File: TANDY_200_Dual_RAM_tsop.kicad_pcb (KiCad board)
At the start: 2 copper layers, 35.6 x 25.4 mm, 5 parts, among them J1 Conn_01x01_Male, J2 TANDY_26-3688, U1 628128_TSOP32, U2 74LVC1G08

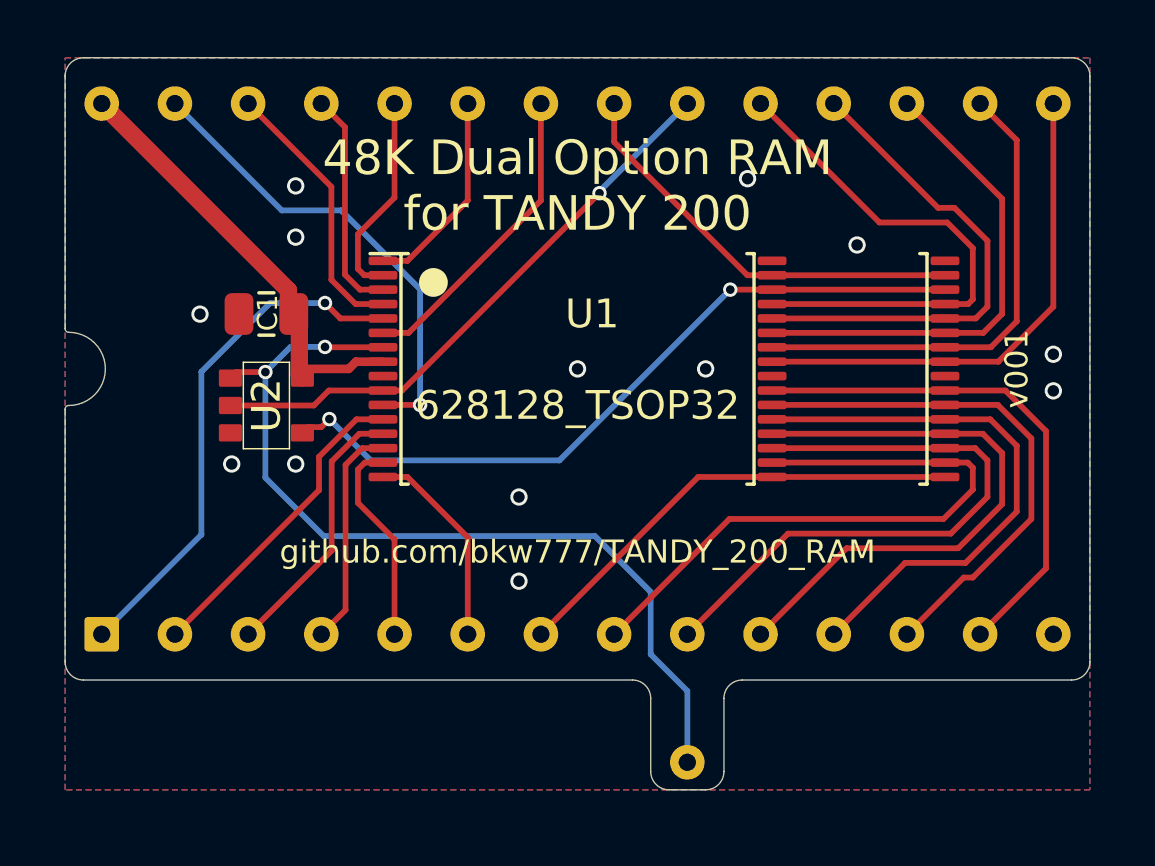
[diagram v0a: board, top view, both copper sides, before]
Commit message: board outlines, ground planes
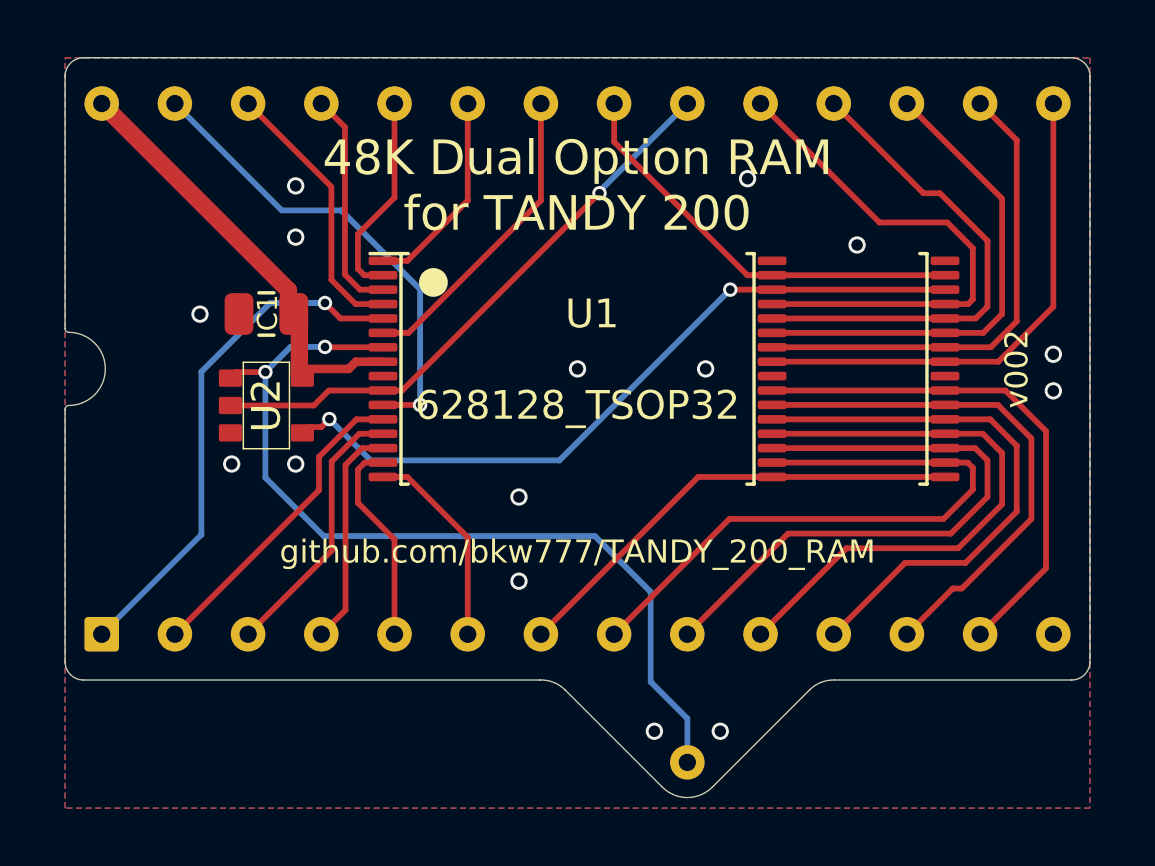
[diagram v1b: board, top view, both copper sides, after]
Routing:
- net GND: vias 13 -> 15
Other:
- board size 35.6 x 25.4 mm -> 35.6 x 25.7 mm
- board text removed: "Row spacing is 725mils, not 700."

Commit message: add single-bank tsop
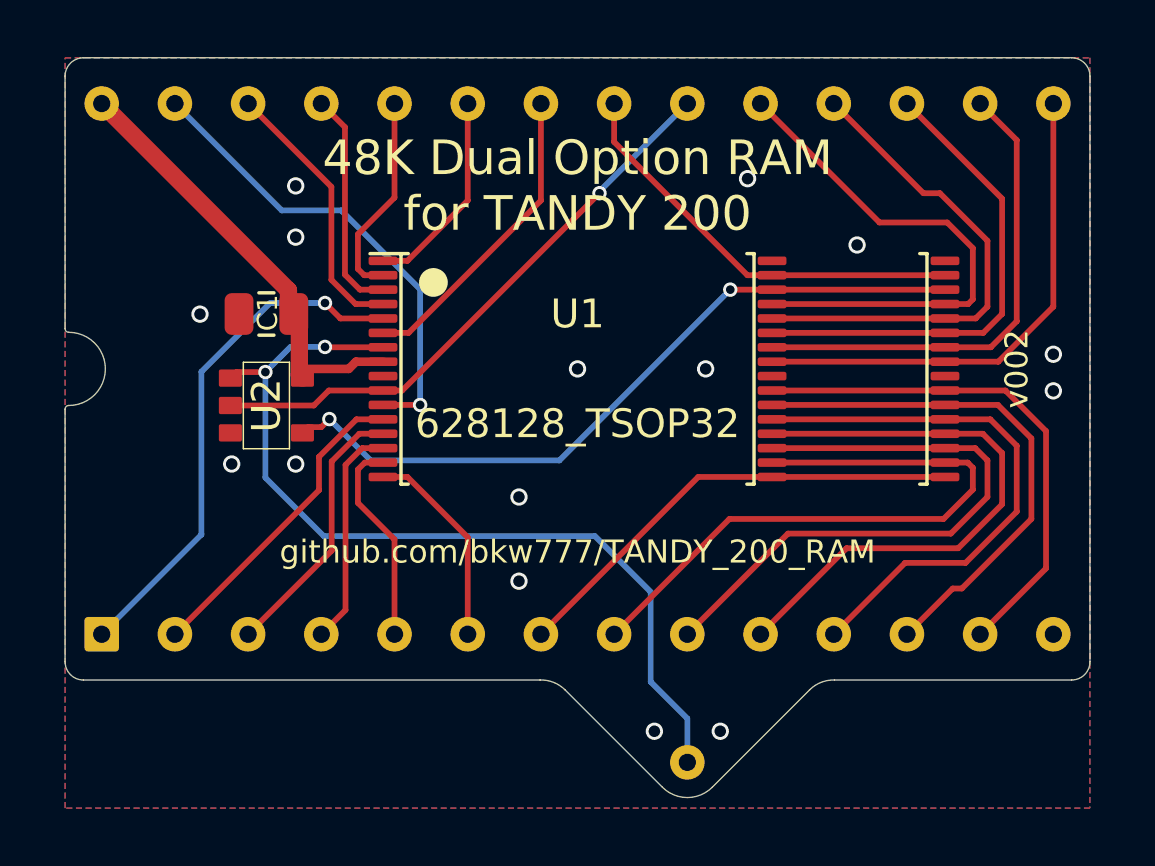
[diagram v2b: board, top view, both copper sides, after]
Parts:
- moved U1 3.00 mm to (150.3, 99.1), turned to 0 degrees

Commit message: ground paths, footprints, sch symbols
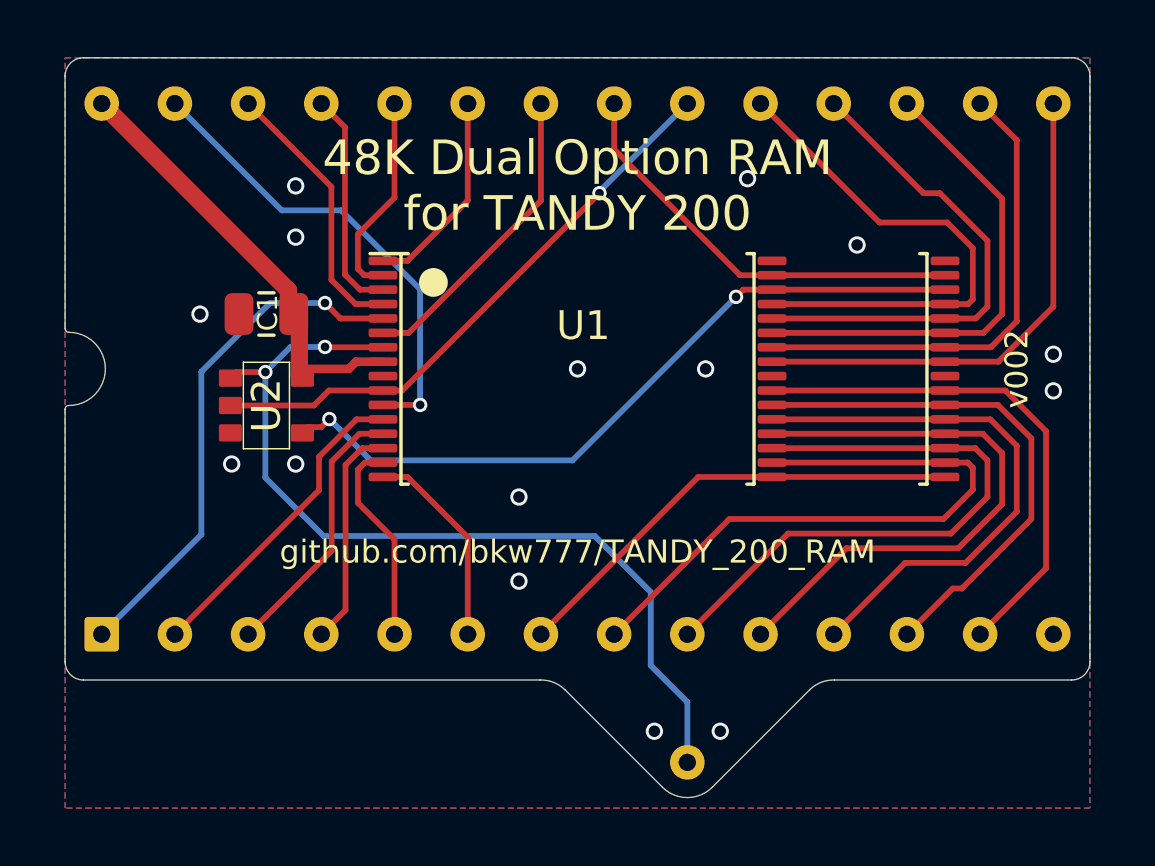
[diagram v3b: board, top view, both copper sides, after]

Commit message: 24k tsop layout and all board outlines expanded slightly
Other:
- board size 35.6 x 25.7 mm -> 36.1 x 25.5 mm
- board text added: "C1: ${91f0851b-88d9-4f00-a08c-ede0bdd24da4:VALUE} U2: ${eda52ffc-b211-43e3-a91c-151a6f13f97e:VALUE} PINS: Mill-Max 3121 or TE 1544210"
- board text removed: "C1: 0.1uF U2: 74LVC1G08 PINS: Mill-Max 3121 or TE 1544210"
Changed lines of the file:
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@@
   (title_block
     (title "TANDY 200 Dual RAM tsop")
-    (date "2022-09-22")
-    (rev "002")
+    (date "2022-10-01")
+    (rev "003")
     (company "b.kenyon.w@gmail.com")
     (comment 1 "github.com/bkw777/TANDY_200_RAM")
@@
     )
   )
-  (gr_line (start 151.993599 113.576099) (end 155.3718 110.197901) (layer "Edge.Cuts") (width 0.01))
-  (gr_arc (start 129.54 100.457) (mid 129.577197 100.367197) (end 129.667 100.33) (layer "Edge.Cuts") (width 0.01))
-  (gr_arc (start 151.993599 113.576099) (mid 151.13 113.933813) (end 150.266401 113.576099) (layer "Edge.Cuts") (width 0.01))
-  (gr_arc (start 165.1 109.22) (mid 164.914013 109.669013) (end 164.465 109.855) (layer "Edge.Cuts") (width 0.01))
-  (gr_arc (start 129.667 97.79) (mid 129.577197 97.752803) (end 129.54 97.663) (layer "Edge.Cuts") (width 0.01))
-  (gr_line (start 129.54 100.457) (end 129.54 109.22) (layer "Edge.Cuts") (width 0.01))
-  (gr_line (start 156.2354 109.855) (end 164.465 109.855) (layer "Edge.Cuts") (width 0.01))
-  (gr_arc (start 129.667 97.79) (mid 130.937 99.06) (end 129.667 100.33) (layer "Edge.Cuts") (width 0.01))
-  (gr_line (start 164.465 88.265) (end 130.175 88.265) (layer "Edge.Cuts") (width 0.01))
-  (gr_line (start 165.1 109.22) (end 165.1 88.9) (layer "Edge.Cuts") (width 0.01))
-  (gr_arc (start 155.3718 110.197901) (mid 155.768182 109.937245) (end 156.2354 109.855) (layer "Edge.Cuts") (width 0.01))
-  (gr_arc (start 129.54 88.9) (mid 129.725987 88.450987) (end 130.175 88.265) (layer "Edge.Cuts") (width 0.01))
-  (gr_line (start 129.54 97.663) (end 129.54 88.9) (layer "Edge.Cuts") (width 0.01))
-  (gr_line (start 146.0246 109.855) (end 130.175 109.855) (layer "Edge.Cuts") (width 0.01))
-  (gr_arc (start 164.465 88.265) (mid 164.914013 88.450987) (end 165.1 88.9) (layer "Edge.Cuts") (width 0.01))
-  (gr_line (start 146.8882 110.197901) (end 150.266401 113.576099) (layer "Edge.Cuts") (width 0.01))
-  (gr_arc (start 130.175 109.855) (mid 129.725987 109.669013) (end 129.54 109.22) (layer "Edge.Cuts") (width 0.01))
-  (gr_arc (start 146.0246 109.855) (mid 146.491818 109.937249) (end 146.8882 110.197901) (layer "Edge.Cuts") (width 0.01))
-  (gr_text "C1: 0.1uF\nU2: 74LVC1G08\nPINS: Mill-Max 3121 or TE 1544210" (at 163.195 103.505) (layer "B.SilkS")
+  (gr_arc (start 129.286 100.457) (mid 129.323197 100.367197) (end 129.413 100.33) (layer "Edge.Cuts") (width 0.01))
+  (gr_line (start 152.032504 113.551504) (end 155.56778 110.02558) (layer "Edge.Cuts") (width 0.01))
+  (gr_arc (start 152.032504 113.551504) (mid 151.13 113.925333) (end 150.227496 113.551504) (layer "Edge.Cuts") (width 0.01))
+  (gr_arc (start 155.56778 110.02558) (mid 155.897394 109.805339) (end 156.2862 109.728001) (layer "Edge.Cuts") (width 0.01))
+  (gr_arc (start 165.354 109.093) (mid 165.168013 109.542013) (end 164.719 109.728) (layer "Edge.Cuts") (width 0.01))
+  (gr_arc (start 145.9738 109.728) (mid 146.362606 109.805338) (end 146.69222 110.02558) (layer "Edge.Cuts") (width 0.01))
+  (gr_arc (start 129.413 97.79) (mid 129.323197 97.752803) (end 129.286 97.663) (layer "Edge.Cuts") (width 0.01))
+  (gr_line (start 129.286 100.457) (end 129.286 109.093) (layer "Edge.Cuts") (width 0.01))
+  (gr_line (start 156.2862 109.728001) (end 164.719 109.728) (layer "Edge.Cuts") (width 0.01))
+  (gr_arc (start 129.413 97.79) (mid 130.683 99.06) (end 129.413 100.33) (layer "Edge.Cuts") (width 0.01))
+  (gr_line (start 164.719 88.392) (end 129.921 88.392) (layer "Edge.Cuts") (width 0.01))
+  (gr_line (start 165.354 109.093) (end 165.354 89.027) (layer "Edge.Cuts") (width 0.01))
+  (gr_line (start 150.227496 113.551504) (end 146.69222 110.02558) (layer "Edge.Cuts") (width 0.01))
+  (gr_arc (start 129.286 89.027) (mid 129.471987 88.577987) (end 129.921 88.392) (layer "Edge.Cuts") (width 0.01))
+  (gr_line (start 129.286 97.663) (end 129.286 89.027) (layer "Edge.Cuts") (width 0.01))
+  (gr_line (start 145.9738 109.728) (end 129.921 109.728) (layer "Edge.Cuts") (width 0.01))
+  (gr_arc (start 164.719 88.392) (mid 165.168013 88.577987) (end 165.354 89.027) (layer "Edge.Cuts") (width 0.01))
+  (gr_arc (start 129.921 109.728) (mid 129.471987 109.542013) (end 129.286 109.093) (layer "Edge.Cuts") (width 0.01))
+  (gr_text "C1: ${91f0851b-88d9-4f00-a08c-ede0bdd24da4:VALUE}\nU2: ${eda52ffc-b211-43e3-a91c-151a6f13f97e:VALUE}\nPINS: Mill-Max 3121 or TE 1544210" (at 163.195 103.505) (layer "B.SilkS")
     (effects (font (size 1 1) (thickness 0.15)) (justify left mirror))
   )
@@
   (segment (start 162.56 104.013) (end 160.782 105.791) (width 0.2) (layer "F.Cu") (net 1))
   (segment (start 158.6865 105.791) (end 156.21 108.2675) (width 0.2) (layer "F.Cu") (net 1))
-  (segment (start 163.068 104.267) (end 160.655 106.68) (width 0.2) (layer "F.Cu") (net 2))
-  (segment (start 160.3375 106.68) (end 158.75 108.2675) (width 0.2) (layer "F.Cu") (net 2))
+  (segment (start 161.905 100.31) (end 163.068 101.473) (width 0.2) (layer "F.Cu") (net 2))
+  (segment (start 163.068 104.267) (end 160.528 106.807) (width 0.2) (layer "F.Cu") (net 2))
+  (segment (start 160.2105 106.807) (end 158.75 108.2675) (width 0.2) (layer "F.Cu") (net 2))
+  (segment (start 160.528 106.807) (end 160.2105 106.807) (width 0.2) (layer "F.Cu") (net 2))
   (segment (start 163.068 101.473) (end 163.068 104.267) (width 0.2) (layer "F.Cu") (net 2))
-  (segment (start 161.905 100.31) (end 163.068 101.473) (width 0.2) (layer "F.Cu") (net 2))
   (segment (start 154.07 100.31) (end 161.905 100.31) (width 0.2) (layer "F.Cu") (net 2))
-  (segment (start 160.655 106.68) (end 160.3375 106.68) (width 0.2) (layer "F.Cu") (net 2))
   (via (at 163.83 99.822) (size 0.6) (drill 0.4) (layers "F.Cu" "B.Cu") (free) (net 3))
   (via (at 137.541 92.71) (size 0.6) (drill 0.4) (layers "F.Cu" "B.Cu") (free) (net 3))
@@
     (polygon
       (pts
-        (xy 165.1 114.3)
-        (xy 129.54 114.3)
-        (xy 129.54 88.265)
-        (xy 165.1 88.265)
+        (xy 165.354 114.3)
+        (xy 129.286 114.3)
+        (xy 129.286 88.265)
+        (xy 165.354 88.265)
       )
     )
@@
     (polygon
       (pts
-        (xy 165.1 114.3)
-        (xy 129.54 114.3)
-        (xy 129.54 88.265)
-        (xy 165.1 88.265)
+        (xy 165.354 114.3)
+        (xy 129.286 114.3)
+        (xy 129.286 88.265)
+        (xy 165.354 88.265)
       )
     )

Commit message: 48k tsop ground pour
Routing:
- net /A14: track 16.5 -> 17.5 mm
- net GND: vias 15 -> 4
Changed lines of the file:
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@@
     (title "TANDY 200 Dual RAM tsop")
     (date "2022-10-01")
-    (rev "003")
+    (rev "004")
     (company "b.kenyon.w@gmail.com")
     (comment 1 "github.com/bkw777/TANDY_200_RAM")
@@
   (segment (start 163.068 101.473) (end 163.068 104.267) (width 0.2) (layer "F.Cu") (net 2))
   (segment (start 154.07 100.31) (end 161.905 100.31) (width 0.2) (layer "F.Cu") (net 2))
-  (via (at 163.83 99.822) (size 0.6) (drill 0.4) (layers "F.Cu" "B.Cu") (free) (net 3))
-  (via (at 137.541 92.71) (size 0.6) (drill 0.4) (layers "F.Cu" "B.Cu") (free) (net 3))
-  (via (at 153.22 92.46) (size 0.6) (drill 0.4) (layers "F.Cu" "B.Cu") (free) (net 3))
-  (via (at 135.32 102.36) (size 0.6) (drill 0.4) (layers "F.Cu" "B.Cu") (free) (net 3))
-  (via (at 145.288 106.426) (size 0.6) (drill 0.4) (layers "F.Cu" "B.Cu") (free) (net 3))
-  (via (at 137.541 102.362) (size 0.6) (drill 0.4) (layers "F.Cu" "B.Cu") (free) (net 3))
-  (via (at 157.02 94.76) (size 0.6) (drill 0.4) (layers "F.Cu" "B.Cu") (free) (net 3))
-  (via (at 163.83 98.552) (size 0.6) (drill 0.4) (layers "F.Cu" "B.Cu") (free) (net 3))
-  (via (at 134.22 97.16) (size 0.6) (drill 0.4) (layers "F.Cu" "B.Cu") (free) (net 3))
-  (via (at 145.288 103.505) (size 0.6) (drill 0.4) (layers "F.Cu" "B.Cu") (free) (net 3))
-  (via (at 152.273 111.633) (size 0.6) (drill 0.4) (layers "F.Cu" "B.Cu") (free) (net 3))
-  (via (at 151.765 99.06) (size 0.6) (drill 0.4) (layers "F.Cu" "B.Cu") (free) (net 3))
-  (via (at 137.541 94.488) (size 0.6) (drill 0.4) (layers "F.Cu" "B.Cu") (free) (net 3))
-  (via (at 149.987 111.633) (size 0.6) (drill 0.4) (layers "F.Cu" "B.Cu") (free) (net 3))
-  (via (at 147.32 99.06) (size 0.6) (drill 0.4) (layers "F.Cu" "B.Cu") (free) (net 3))
+  (via (at 163.83 99.06) (size 0.6) (drill 0.4) (layers "F.Cu" "B.Cu") (free) (net 3))
+  (via (at 134.62 95.885) (size 0.6) (drill 0.4) (layers "F.Cu" "B.Cu") (free) (net 3))
+  (via (at 137.414 102.489) (size 0.6) (drill 0.4) (layers "F.Cu" "B.Cu") (free) (net 3))
+  (via (at 152.4 99.314) (size 0.6) (drill 0.4) (layers "F.Cu" "B.Cu") (free) (net 3))
   (segment (start 163.576 101.219) (end 163.576 105.9815) (width 0.2) (layer "F.Cu") (net 4))
   (segment (start 163.576 105.9815) (end 161.29 108.2675) (width 0.2) (layer "F.Cu") (net 4))
@@
   (segment (start 154.6225 104.775) (end 151.13 108.2675) (width 0.2) (layer "F.Cu") (net 21))
   (segment (start 161.544 103.505) (end 160.274 104.775) (width 0.2) (layer "F.Cu") (net 21))
-  (segment (start 140.57 100.31) (end 141.859 100.31) (width 0.2) (layer "F.Cu") (net 22))
-  (via (at 141.859 100.31) (size 0.5) (drill 0.3) (layers "F.Cu" "B.Cu") (net 22))
-  (segment (start 139.12 93.56) (end 137.0575 93.56) (width 0.2) (layer "B.Cu") (net 22))
-  (segment (start 137.0575 93.56) (end 133.35 89.8525) (width 0.2) (layer "B.Cu") (net 22))
-  (segment (start 141.859 100.31) (end 141.859 96.299) (width 0.2) (layer "B.Cu") (net 22))
-  (segment (start 141.859 96.299) (end 139.12 93.56) (width 0.2) (layer "B.Cu") (net 22))
+  (segment (start 142.748 99.314) (end 141.752 100.31) (width 0.2) (layer "F.Cu") (net 22))
+  (segment (start 141.752 100.31) (end 140.57 100.31) (width 0.2) (layer "F.Cu") (net 22))
+  (via (at 142.748 99.314) (size 0.5) (drill 0.3) (layers "F.Cu" "B.Cu") (net 22))
+  (segment (start 136.8425 93.345) (end 133.35 89.8525) (width 0.2) (layer "B.Cu") (net 22))
+  (segment (start 142.748 96.52) (end 139.573 93.345) (width 0.2) (layer "B.Cu") (net 22))
+  (segment (start 139.573 93.345) (end 136.8425 93.345) (width 0.2) (layer "B.Cu") (net 22))
+  (segment (start 142.748 99.314) (end 142.748 96.52) (width 0.2) (layer "B.Cu") (net 22))
   (segment (start 156.6545 105.283) (end 153.67 108.2675) (width 0.2) (layer "F.Cu") (net 23))
   (segment (start 161.381 101.31) (end 162.052 101.981) (width 0.2) (layer "F.Cu") (net 23))
@@
   (via (at 136.49 99.17) (size 0.5) (drill 0.3) (layers "F.Cu" "B.Cu") (net 25))
   (via (at 138.557 98.298) (size 0.5) (drill 0.3) (layers "F.Cu" "B.Cu") (free) (net 25))
+  (segment (start 149.86 109.35) (end 151.13 110.62) (width 0.2) (layer "B.Cu") (net 25))
+  (segment (start 138.557 98.298) (end 137.362 98.298) (width 0.2) (layer "B.Cu") (net 25))
+  (segment (start 148.343 105.283) (end 149.86 106.8) (width 0.2) (layer "B.Cu") (net 25))
+  (segment (start 138.938 105.283) (end 148.343 105.283) (width 0.2) (layer "B.Cu") (net 25))
+  (segment (start 137.362 98.298) (end 136.49 99.17) (width 0.2) (layer "B.Cu") (net 25))
+  (segment (start 136.49 99.17) (end 136.49 102.835) (width 0.2) (layer "B.Cu") (net 25))
+  (segment (start 149.86 106.8) (end 149.86 109.35) (width 0.2) (layer "B.Cu") (net 25))
+  (segment (start 136.49 102.835) (end 138.938 105.283) (width 0.2) (layer "B.Cu") (net 25))
   (segment (start 151.13 110.62) (end 151.13 112.7125) (width 0.2) (layer "B.Cu") (net 25))
-  (segment (start 149.86 109.35) (end 151.13 110.62) (width 0.2) (layer "B.Cu") (net 25))
-  (segment (start 138.515 104.86) (end 147.92 104.86) (width 0.2) (layer "B.Cu") (net 25))
-  (segment (start 138.557 98.298) (end 137.362 98.298) (width 0.2) (layer "B.Cu") (net 25))
-  (segment (start 137.362 98.298) (end 136.49 99.17) (width 0.2) (layer "B.Cu") (net 25))
-  (segment (start 136.49 102.835) (end 138.515 104.86) (width 0.2) (layer "B.Cu") (net 25))
-  (segment (start 147.92 104.86) (end 149.86 106.8) (width 0.2) (layer "B.Cu") (net 25))
-  (segment (start 149.86 106.8) (end 149.86 109.35) (width 0.2) (layer "B.Cu") (net 25))
-  (segment (start 136.49 99.17) (end 136.49 102.835) (width 0.2) (layer "B.Cu") (net 25))
   (segment (start 139.093 97.31) (end 140.57 97.31) (width 0.2) (layer "F.Cu") (net 26))
   (segment (start 138.557 96.774) (end 139.093 97.31) (width 0.2) (layer "F.Cu") (net 26))
@@
   (segment (start 140.57 97.81) (end 141.458 97.81) (width 0.2) (layer "F.Cu") (net 29))
   (segment (start 146.05 93.218) (end 146.05 89.8525) (width 0.2) (layer "F.Cu") (net 29))
-  (segment (start 153.07 96.31) (end 152.82 96.56) (width 0.2) (layer "F.Cu") (net 30))
   (segment (start 137.975 101.08) (end 137.775 101.28) (width 0.2) (layer "F.Cu") (net 30))
   (segment (start 154.07 96.31) (end 160.07 96.31) (width 0.2) (layer "F.Cu") (net 30))
-  (segment (start 154.07 96.31) (end 153.07 96.31) (width 0.2) (layer "F.Cu") (net 30))
   (segment (start 138.43 101.08) (end 137.975 101.08) (width 0.2) (layer "F.Cu") (net 30))
+  (segment (start 147.32 99.06) (end 150.07 96.31) (width 0.2) (layer "F.Cu") (net 30))
+  (segment (start 150.07 96.31) (end 154.07 96.31) (width 0.2) (layer "F.Cu") (net 30))
   (segment (start 138.71 100.8) (end 138.43 101.08) (width 0.2) (layer "F.Cu") (net 30))
-  (via (at 152.82 96.56) (size 0.5) (drill 0.3) (layers "F.Cu" "B.Cu") (free) (net 30))
+  (via (at 147.32 99.06) (size 0.5) (drill 0.3) (layers "F.Cu" "B.Cu") (free) (net 30))
   (via (at 138.71 100.8) (size 0.5) (drill 0.3) (layers "F.Cu" "B.Cu") (free) (net 30))
-  (segment (start 152.82 96.56) (end 147.145 102.235) (width 0.2) (layer "B.Cu") (net 30))
+  (segment (start 147.32 99.06) (end 144.145 102.235) (width 0.2) (layer "B.Cu") (net 30))
   (segment (start 140.145 102.235) (end 138.71 100.8) (width 0.2) (layer "B.Cu") (net 30))
-  (segment (start 147.145 102.235) (end 140.145 102.235) (width 0.2) (layer "B.Cu") (net 30))
+  (segment (start 144.145 102.235) (end 140.145 102.235) (width 0.2) (layer "B.Cu") (net 30))
   (zone (net 3) (net_name "GND") (layer "F.Cu") (hatch edge 0.508)
     (connect_pads (clearance 0.2))
